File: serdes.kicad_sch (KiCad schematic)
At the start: 11 parts

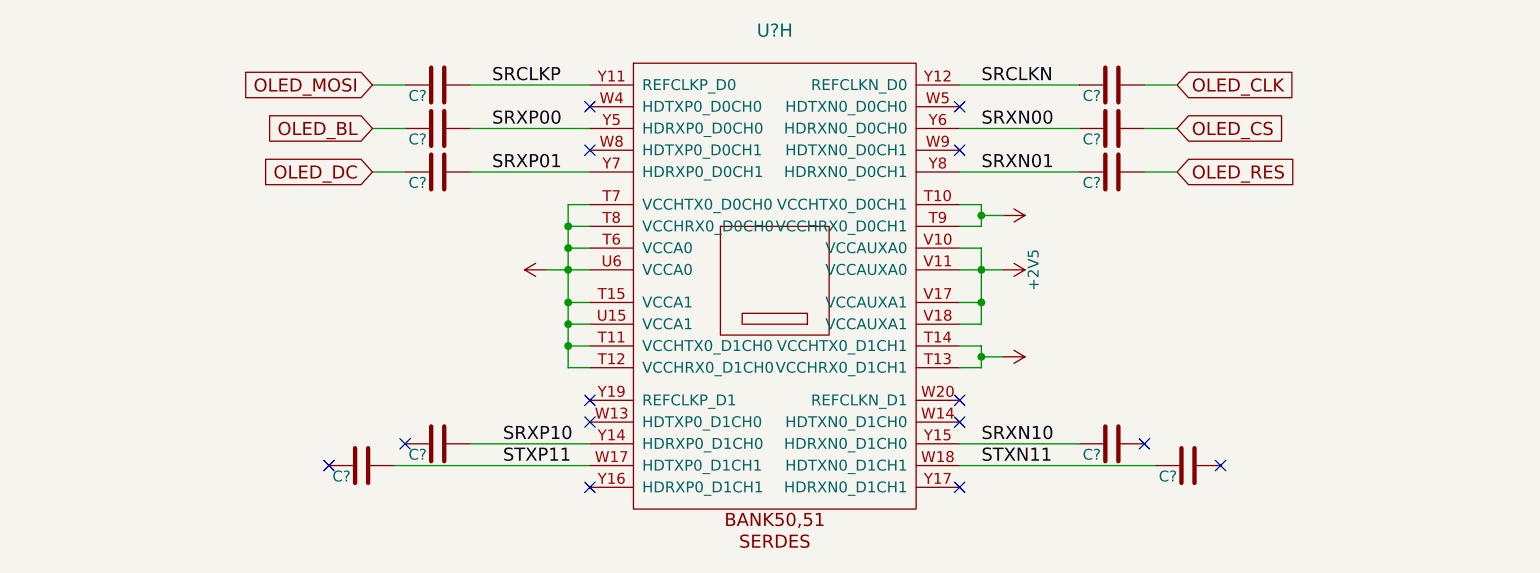
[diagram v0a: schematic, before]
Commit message: Full SerDes is now connected
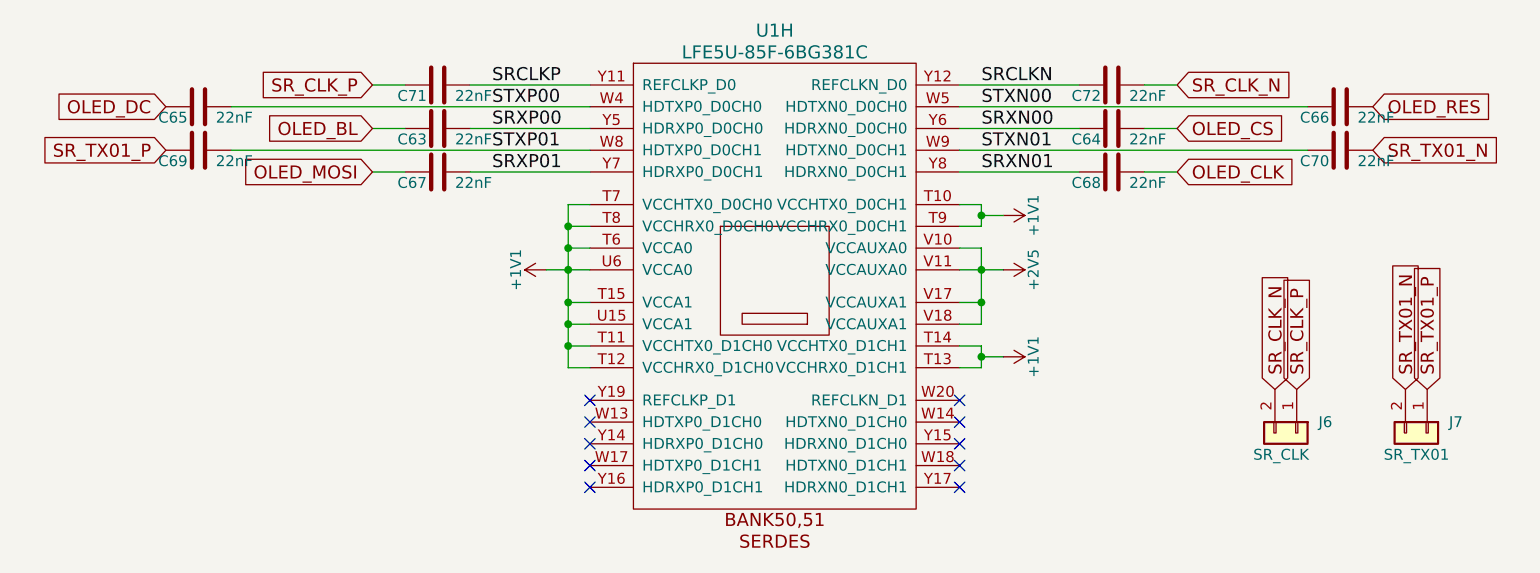
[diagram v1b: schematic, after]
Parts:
- added J6: SR_CLK, Connector_PinSocket_1.00mm:PinSocket_1x02_P1.00mm_Vertical, symbol Connector_Generic:Conn_01x02
- added J7: SR_TX01, Connector_PinSocket_1.00mm:PinSocket_1x02_P1.00mm_Vertical, symbol Connector_Generic:Conn_01x02
- C63, C64, C65, C66, C67, C68, C69, C70, C71, C72: renamed from C?; value (none) -> 22nF; footprint (none) -> Capacitor_SMD:C_0603_1608Metric
- U1: renamed from U?; value (none) -> LFE5U-85F-6BG381C; footprint (none) -> lfe5bg381:BGA-381_pitch0.8mm_dia0.4mm; Digike_y2 220-2071-ND -> (none); Digikey 220-2177-ND -> (none); Koncar FU004 -> (none); LCSC C446029 -> (none); LowCost 842-LFE5U12F6BG381C -> (none); MFG1 Lattice -> (none); MFG2 Lattice -> (none); MNF2_URL www.latticesemi.com -> (none); MP_N2 LFE5U-12F-6BG381C -> (none); Mouser 842-LFE5U85F6BG381C -> (none); Side T -> (none); price100_Mouse 22.82$ -> (none)
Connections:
- net SRCLKN: now also C72.1; no longer C68.1
- net SRCLKP: now also C71.2; no longer C67.2
- net SRXN01: now also C68.1; no longer C66.1
- net SRXP01: now also C67.2; no longer C65.2
- net SR_TX01_N: now reaches C70.2
- net SR_TX01_N: now also J7.2 (Pin_2)
- net SR_TX01_P: now reaches C69.1
- net SR_TX01_P: now also J7.1 (Pin_1)
- net SR_CLK_P: now reaches C71.1
- net SR_CLK_P: now also J6.1 (Pin_1)
- net SR_CLK_N: now reaches C72.2
- net SR_CLK_N: now also J6.2 (Pin_2)
- net STXP00: now reaches U1.W4 (HDTXP0_D0CH0)
- net STXP00: now also C65.2
- net STXN00: now reaches U1.W5 (HDTXN0_D0CH0)
- net STXN00: now also C66.1
- net STXP01: now reaches U1.W8 (HDTXP0_D0CH1)
- net STXP01: now also C69.2
- net STXN01: now reaches U1.W9 (HDTXN0_D0CH1)
- net STXN01: now also C70.1
- net SRXN10: no longer names the net of U1.Y15 (HDRXN0_D1CH0)
- net SRXN10: no longer C70.1
- net SRXP10: no longer names the net of U1.Y14 (HDRXP0_D1CH0)
- net SRXP10: no longer C69.2
- net STXN11: no longer names the net of U1.W18 (HDTXN0_D1CH1)
- net STXN11: no longer C72.1
- net STXP11: no longer names the net of U1.W17 (HDTXP0_D1CH1)
- net STXP11: no longer C71.2
- no-connect marks 14 -> 10
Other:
- moved on the sheet: C65, C66, C67, C68, C69, C70, C71, C72
